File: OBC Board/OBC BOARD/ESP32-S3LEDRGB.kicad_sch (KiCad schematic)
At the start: 8 parts, among them Q1 FMMT619TA, Q2 FMMT619TA

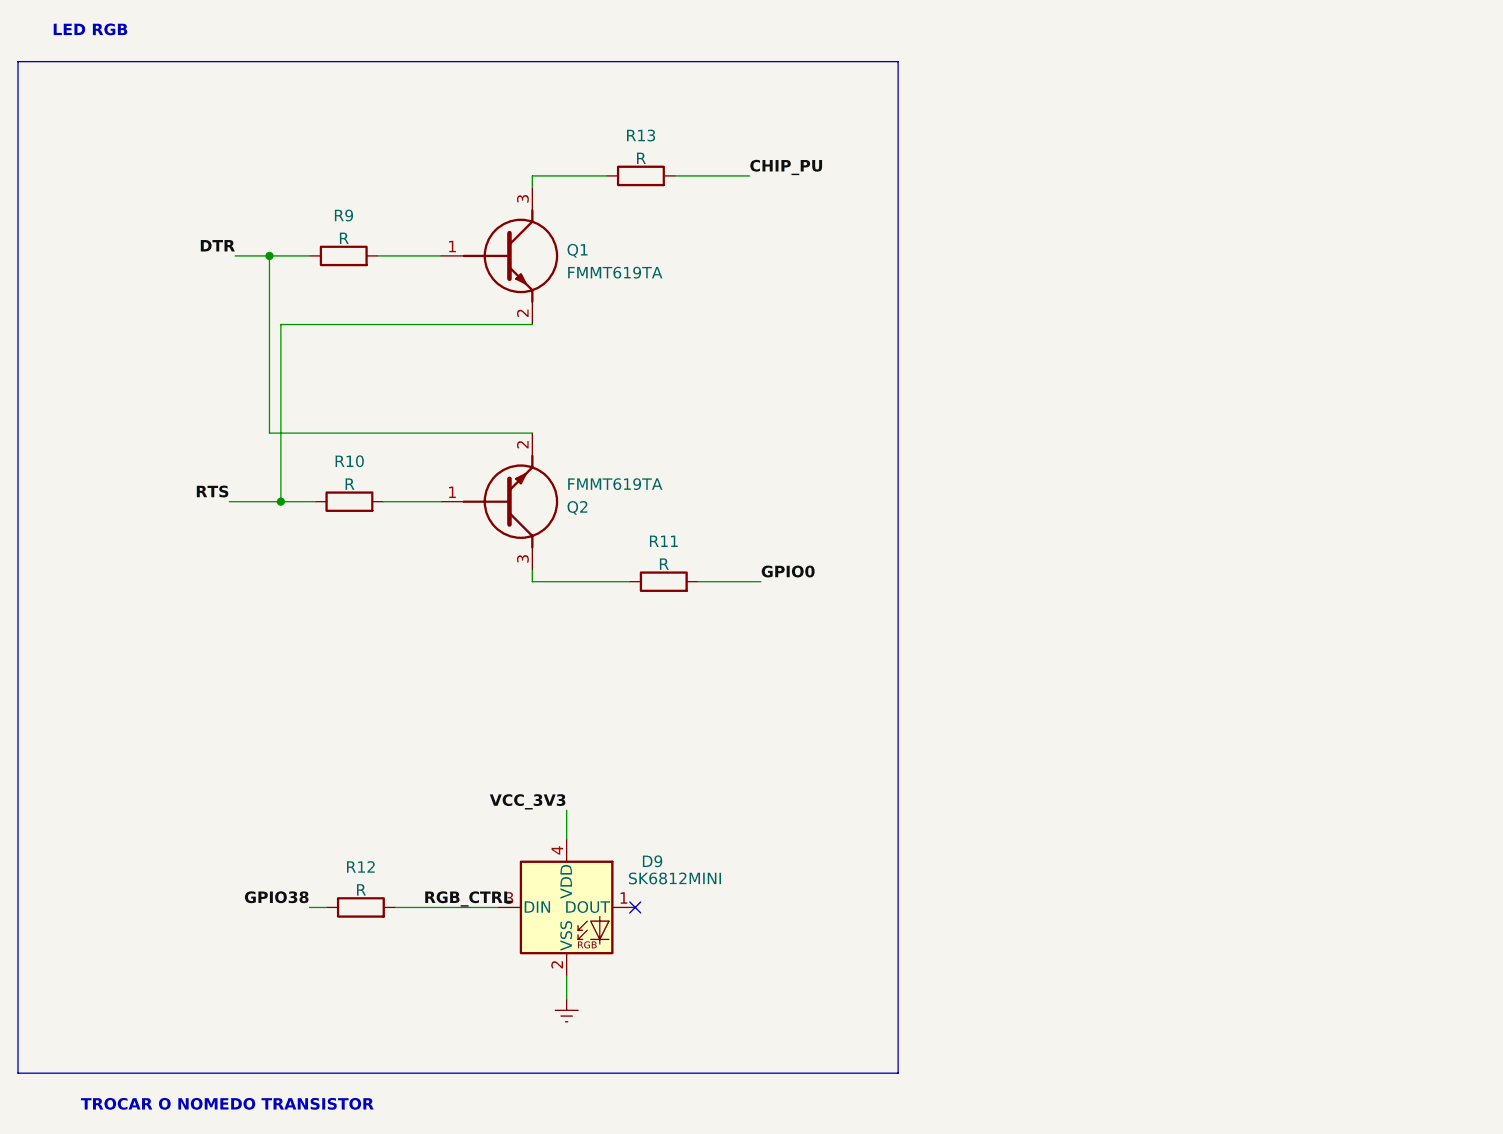
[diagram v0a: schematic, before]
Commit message: Realização do diagrama de blocos, test points, padronização e mudança dos caminhos das bibliotecas de footprints e simbolos
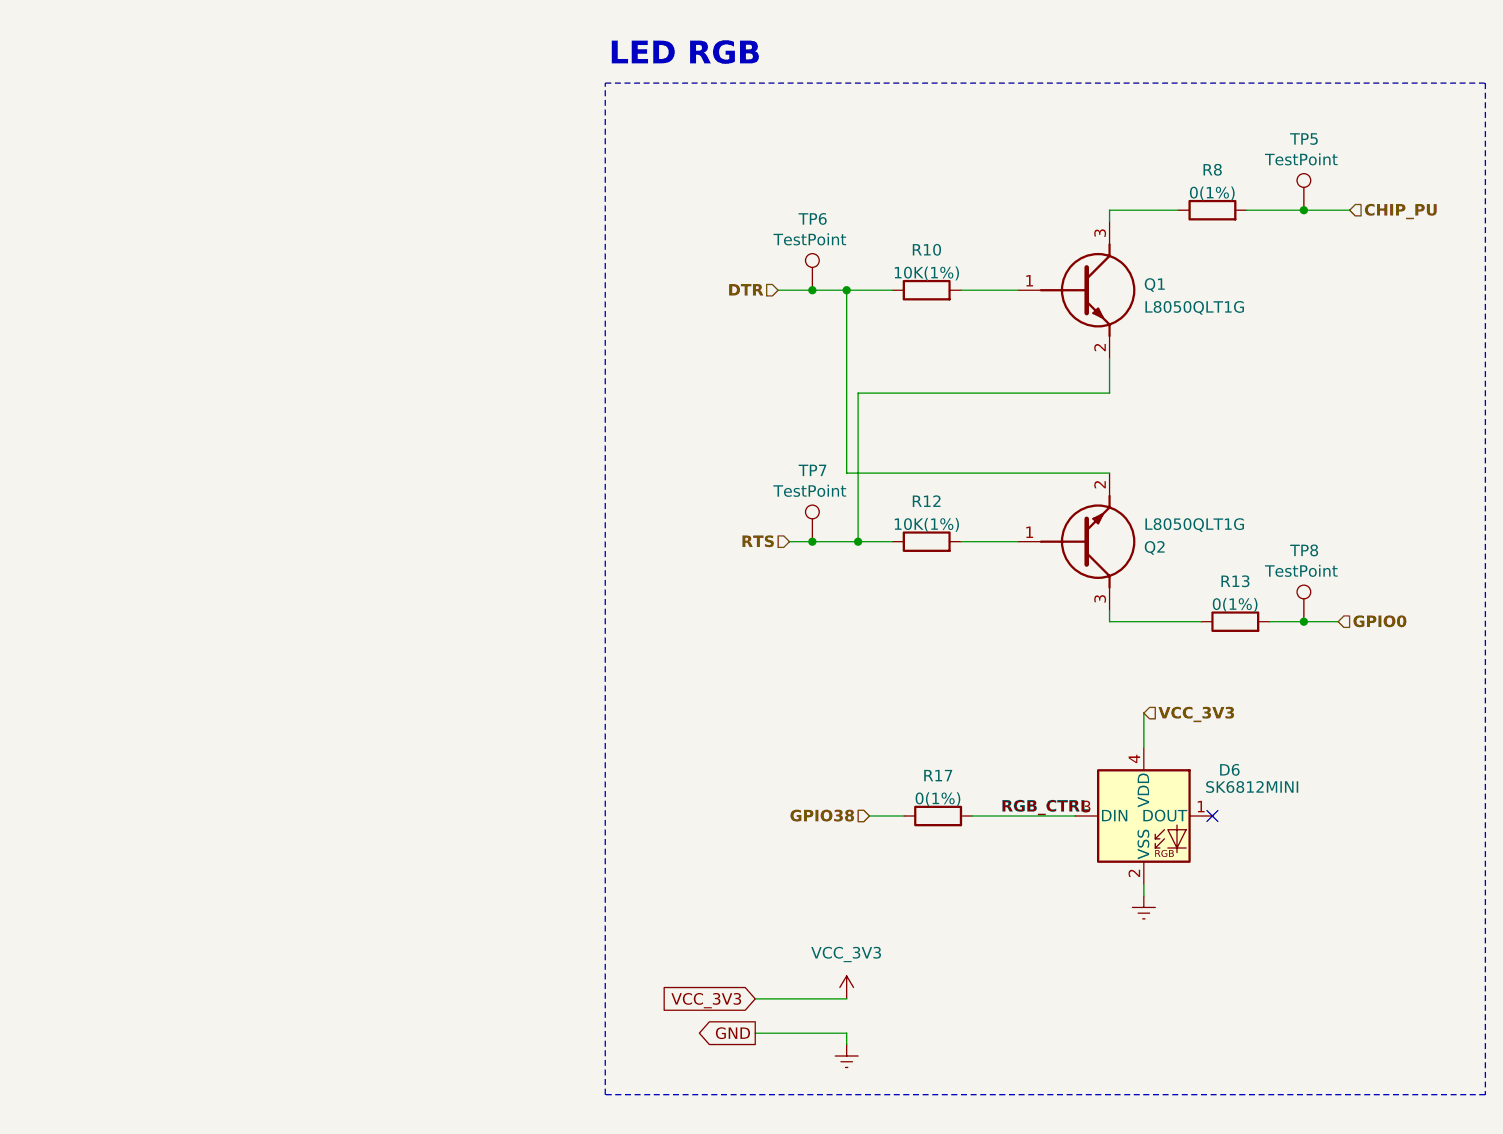
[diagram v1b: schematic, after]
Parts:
- added TP5, TP6, TP7, TP8: TestPoint, TestPoint:TestPoint_Pad_4.0x4.0mm, symbol Connector:TestPoint
- Q1, Q2: value FMMT619TA -> L8050QLT1G; footprint SOT96P240X120-3N -> SOT96P240X120-3N:SOT96P240X120-3N
- R10: renamed from R9; value R -> 10K(1%); footprint (none) -> Resistor_SMD:R_0603_1608Metric
- R12: renamed from R10; value R -> 10K(1%); footprint (none) -> Resistor_SMD:R_0603_1608Metric
- R13: renamed from R11; value R -> 0(1%); footprint (none) -> Resistor_SMD:R_0603_1608Metric
- R17: renamed from R12; value R -> 0(1%); footprint (none) -> Resistor_SMD:R_0603_1608Metric
- R8: renamed from R13; value R -> 0(1%); footprint (none) -> Resistor_SMD:R_0603_1608Metric
- renumbered D9 to D6
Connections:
- net CHIP_PU: now also TP5.1
- net DTR: now also TP6.1
- net GPIO0: now also TP8.1
- net RTS: now also TP7.1
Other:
- note removed: "TROCAR O NOMEDO TRANSISTOR"
- title: ICARUS-2 OBCH -> ICARUS-2 OBDH
- moved on the sheet: D6, Q1, Q2, R10, R12, R13, R17, R8
